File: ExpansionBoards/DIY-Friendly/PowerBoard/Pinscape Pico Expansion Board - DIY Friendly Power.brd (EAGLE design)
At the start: 138 x 100 mm, 79 parts, among them IC1 UCC27524P, IC10 ULN2803A, IC11 ULN2803A, IC12 ULN2803A, IC13 DS1307+, IC2 UCC27524P, IC3 UCC27524P, IC4 UCC27524P, IC5 UCC27524P, IC6 UCC27524P, IC7 UCC27524P, IC8 UCC27524P, IC9 ULN2803A, J1 640445-4, J15 SSQ-108-02-T-S-RA, J2 640445-9, J3 640445-9, J4 1-640456-0, J5 1-640456-0, J6 1-640456-0, J7 1-640456-0, Q1 FDPF085N10A, Q10 FDPF085N10A, Q11 FDPF085N10A, Q12 FDPF085N10A, Q13 FDPF085N10A, Q14 FDPF085N10A, Q15 FDPF085N10A, Q16 FDPF085N10A, Q2 FDPF085N10A, Q3 FDPF085N10A, Q4 FDPF085N10A, Q5 FDPF085N10A, Q6 FDPF085N10A, Q7 FDPF085N10A, Q8 FDPF085N10A, Q9 FDPF085N10A, Y1 ECS-.327-12.5-13X-C

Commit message: expansion board improvements
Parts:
- J1: value 640445-4 -> 640445-6; device SamacSys_Parts:SHDR4W117P0X396_1X4_1585X762X1 -> SamacSys_Parts:SHDR6W183P0X396_1X6_2377X762X1
- moved J1 13.5 mm to (105.8, 93.7), turned to 0 degrees
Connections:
- net 12V: now also J1.5; no longer J1.3
- net 5V: now also J1.6; no longer J1.4
- net GND: now also J1.3, J1.4
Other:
- board text added: "REV 20250106"
- board text removed: "REV 20241208"
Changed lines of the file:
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@@
 PICO</text>
 <text x="8.5" y="52.5" size="1.1" layer="25" ratio="20" rot="SR0" align="center">DIY POWER BOARD</text>
-<text x="8.4" y="51" size="1.1" layer="25" ratio="15" rot="SR0" align="center">REV 20241208</text>
+<text x="8.4" y="51" size="1.1" layer="25" ratio="15" rot="SR0" align="center">REV 20250106</text>
 <text x="29.5" y="98.3" size="1.8" layer="25" ratio="15" rot="SR0" align="center">HIGH POWER OUTPUTS 13-20</text>
 <text x="33.8" y="53.5" size="1.8" layer="25" ratio="15" rot="SR0" align="center">PICO 1</text>
@@
 <text x="80.7" y="98.4" size="1.8" layer="25" ratio="15" rot="SR0" align="center">HIGH POWER OUTPUTS 21-28</text>
 <text x="80.4" y="87.8" size="2.5" layer="25" ratio="15" rot="SR270" align="center">X</text>
-<text x="119.4" y="98.2" size="1.8" layer="25" ratio="15" rot="SR0" align="center">2ND PSU</text>
+<text x="116.5" y="98.4" size="1.8" layer="25" ratio="15" rot="SR0" align="center">2ND PSU</text>
 <text x="122.3" y="87.7" size="1.5" layer="25" ratio="15" rot="SR0" align="center">12V</text>
-<text x="117.6" y="87.7" size="1.5" layer="25" ratio="15" rot="SR0" align="center">GND</text>
+<text x="110" y="87.8" size="1.2" layer="25" ratio="15" rot="SR0" align="center">GND</text>
 <text x="12.4" y="31.4" size="1.8" layer="25" ratio="15" rot="SR270" align="center">TO MAIN BOARD</text>
 <text x="136.2" y="76.7" size="1.8" layer="25" ratio="15" rot="SR90" align="center">LAMPS 1-8</text>
@@
 <text x="91.5" y="9.6" size="1.2" layer="25" ratio="15" rot="SR0" align="center">32</text>
 <text x="127.6" y="35.5" size="1.4" layer="25" ratio="15" rot="SR0" align="center">5V</text>
-<text x="112.9" y="87.7" size="1.5" layer="25" ratio="15" rot="SR0" align="center">GND</text>
+<text x="105.7" y="87.8" size="1.2" layer="25" ratio="15" rot="SR0" align="center">GND</text>
 <text x="101.6" y="49.3" size="2" layer="21" align="center">CR2032</text>
 <text x="18" y="88.3" size="1.2" layer="25" ratio="15" rot="SR0" align="center">14</text>
@@
 <text x="99.3" y="9.6" size="1.2" layer="25" ratio="15" rot="SR0" align="center">30</text>
 <text x="96.8" y="9.6" size="1.2" layer="25" ratio="15" rot="SR0" align="center">31</text>
+<text x="114" y="87.8" size="1.2" layer="25" ratio="15" rot="SR0" align="center">GND</text>
+<text x="118" y="87.8" size="1.2" layer="25" ratio="15" rot="SR0" align="center">GND</text>
 </plain>
 <attributes>
@@
 <attribute name="VALUE" x="81.478" y="62.667" size="0.6" layer="27" ratio="10" rot="R180"/>
 </element>
-<element name="J1" library="SamacSys_Parts" package="SHDR4W117P0X396_1X4_1585X762X1" value="640445-4" x="119.3" y="93.7" smashed="yes" rot="R180">
-<attribute name="MOUSER_PRICE-STOCK" value="https://www.mouser.co.uk/ProductDetail/TE-Connectivity-AMP/640445-4?qs=P8zzrVhehatZnQ7HMsIjxw%3D%3D" x="119.3" y="93.7" size="1" layer="27" rot="R180" display="off"/>
-<attribute name="HEIGHT" value="13.716mm" x="119.3" y="93.7" size="1" layer="27" rot="R180" display="off"/>
-<attribute name="MANUFACTURER_PART_NUMBER" value="640445-4" x="119.3" y="93.7" size="1" layer="27" rot="R180" display="off"/>
-<attribute name="MANUFACTURER_NAME" value="TE Connectivity" x="119.3" y="93.7" size="1" layer="27" rot="R180" display="off"/>
-<attribute name="MOUSER_PART_NUMBER" value="571-6404454" x="119.3" y="93.7" size="1" layer="27" rot="R180" display="off"/>
-<attribute name="DESCRIPTION" value="Conn Wire to Board HDR 4 POS 3.96mm Solder ST Top Entry Thru-Hole Package" x="119.3" y="93.7" size="1" layer="27" rot="R180" display="off"/>
-<attribute name="NAME" x="122.3" y="91.4" size="1.27" layer="25" rot="R270" align="center"/>
-<attribute name="VALUE" x="114.5" y="91.2" size="0.8" layer="27" rot="R180" align="center"/>
+<element name="J1" library="SamacSys_Parts" package="SHDR6W183P0X396_1X6_2377X762X1" value="640445-6" x="105.8" y="93.7" smashed="yes">
+<attribute name="MOUSER_PRICE-STOCK" value="https://www.mouser.com/Search/Refine.aspx?Keyword=571-6404456" x="105.8" y="93.7" size="1" layer="27" display="off"/>
+<attribute name="HEIGHT" value="11.049mm" x="105.8" y="93.7" size="1" layer="27" display="off"/>
+<attribute name="MANUFACTURER_PART_NUMBER" value="640445-6" x="105.8" y="93.7" size="1" layer="27" display="off"/>
+<attribute name="MANUFACTURER_NAME" value="TE Connectivity" x="105.8" y="93.7" size="1" layer="27" display="off"/>
+<attribute name="MOUSER_PART_NUMBER" value="571-6404456" x="105.8" y="93.7" size="1" layer="27" display="off"/>
+<attribute name="DESCRIPTION" value="6 way friction lock header,3.96mm pitch" x="105.8" y="93.7" size="1" layer="27" display="off"/>
+<attribute name="NAME" x="105" y="97.8" size="1.27" layer="25" rot="R180" align="center"/>
+<attribute name="VALUE" x="110.6" y="96.2" size="0.8" layer="27" align="center"/>
 </element>
 <element name="J15" library="SamacSys_Parts" package="RHDRRA8W64P254_1X8_2083X851X24" value="SSQ-108-02-T-S-RA" x="9.9" y="40.1" smashed="yes" rot="R90">
@@
 <via x="106.8" y="45.4" extent="1-16" drill="0.45"/>
 <via x="105.9" y="27.1" extent="1-16" drill="0.45"/>
+<contactref element="J1" pad="3"/>
+<contactref element="J1" pad="4"/>
+<polygon width="0.3" layer="1" thermals="no">
+<vertex x="103.6" y="95.7"/>
+<vertex x="119.6" y="95.7"/>
+<vertex x="119.6" y="91.6"/>
+<vertex x="103.6" y="91.6"/>
+</polygon>
+<polygon width="0.3" layer="16" thermals="no">
+<vertex x="103.6" y="91.6"/>
+<vertex x="119.6" y="91.6"/>
+<vertex x="119.6" y="95.7"/>
+<vertex x="103.6" y="95.7"/>
+</polygon>
+<polygon width="0.3" layer="16" thermals="no">
+<vertex x="12" y="23.5"/>
+<vertex x="12" y="41.5"/>
+<vertex x="7.9" y="41.5"/>
+<vertex x="7.9" y="23.5"/>
+</polygon>
+<polygon width="0.3" layer="1" thermals="no">
+<vertex x="7.9" y="23.6"/>
+<vertex x="7.9" y="41.5"/>
+<vertex x="12" y="41.5"/>
+<vertex x="12" y="23.6"/>
+</polygon>
 </signal>
 <signal name="SDA">
@@
 <wire x1="128.7" y1="12.7" x2="121.4" y2="5.4" width="2" layer="16"/>
 <wire x1="114.33" y1="5.4" x2="121.4" y2="5.4" width="2" layer="16"/>
-<contactref element="J1" pad="4"/>
-<wire x1="125.246" y1="93.7" x2="125.246" y2="91.984" width="2" layer="1"/>
-<wire x1="125.246" y1="91.984" x2="129.4" y2="87.83" width="2" layer="1"/>
 <contactref element="IC13" pad="8"/>
+<wire x1="125.6" y1="91.63" x2="129.4" y2="87.83" width="2" layer="1"/>
 <wire x1="58.1" y1="0.6" x2="112.3" y2="0.6" width="0.4" layer="1"/>
 <wire x1="112.3" y1="0.6" x2="114.33" y2="2.63" width="0.4" layer="1"/>
@@
 <wire x1="52.7" y1="6" x2="58.1" y2="0.6" width="0.4" layer="1"/>
 <wire x1="53.99" y1="24.39" x2="52.7" y2="23.1" width="0.4" layer="1"/>
+<contactref element="J1" pad="6"/>
+<wire x1="125.6" y1="93.7" x2="125.6" y2="91.63" width="2" layer="1"/>
 </signal>
 <signal name="SDA1">
@@
 <wire x1="70.09" y1="66.72" x2="71.5" y2="68.13" width="1" layer="1"/>
 <wire x1="80.5" y1="68.13" x2="80.5" y2="66.17" width="1" layer="1"/>
-<contactref element="J1" pad="3"/>
 <contactref element="IC7" pad="6"/>
 <contactref element="IC7" pad="8"/>
@@
 <wire x1="107.73" y1="68.13" x2="108.7" y2="69.1" width="1" layer="1"/>
 <wire x1="108.7" y1="69.1" x2="108.7" y2="76.7" width="1" layer="1"/>
-<wire x1="108.7" y1="76.7" x2="120.4" y2="88.4" width="1" layer="1"/>
-<wire x1="120.4" y1="88.4" x2="120.624" y2="88.624" width="1" layer="1"/>
-<wire x1="121.284" y1="93.7" x2="121.284" y2="89.284" width="1" layer="1"/>
-<wire x1="121.284" y1="89.284" x2="120.624" y2="88.624" width="1" layer="1"/>
+<wire x1="108.7" y1="76.7" x2="120.95" y2="88.95" width="1" layer="1"/>
+<contactref element="J1" pad="5"/>
+<wire x1="120.95" y1="88.95" x2="121.284" y2="89.284" width="1" layer="1"/>
+<wire x1="121.64" y1="93.7" x2="121.64" y2="89.64" width="1" layer="1"/>
+<wire x1="121.64" y1="89.64" x2="121.284" y2="89.284" width="1" layer="1"/>
 </signal>
 <signal name="OUTCTL14">
@@
 <wire x1="99.64" y1="81.4" x2="102.1" y2="81.4" width="2.5" layer="1"/>
 <wire x1="102.1" y1="81.4" x2="103" y2="82.3" width="2.5" layer="1"/>
-<wire x1="103" y1="82.3" x2="103" y2="87" width="2.5" layer="1"/>
-<wire x1="96.494" y1="93.7" x2="96.494" y2="91.706" width="2.5" layer="1"/>
-<wire x1="96.494" y1="91.706" x2="99.5" y2="88.7" width="2.5" layer="1"/>
-<wire x1="99.5" y1="88.7" x2="101.3" y2="88.7" width="2.5" layer="1"/>
-<wire x1="101.3" y1="88.7" x2="103" y2="87" width="2.5" layer="1"/>
+<wire x1="96.494" y1="93.7" x2="96.494" y2="89.706" width="2.5" layer="1"/>
+<wire x1="96.494" y1="89.706" x2="99.4" y2="86.8" width="2.5" layer="1"/>
+<wire x1="99.4" y1="86.8" x2="101.3" y2="86.8" width="2.5" layer="1"/>
+<wire x1="101.3" y1="86.8" x2="103" y2="85.1" width="2.5" layer="1"/>
+<wire x1="103" y1="82.3" x2="103" y2="85.1" width="2.5" layer="1"/>
 </signal>
 <signal name="OUT28">
@@
 <wire x1="106.44" y1="81.4" x2="108.5" y2="81.4" width="2.5" layer="1"/>
 <wire x1="108.5" y1="81.4" x2="109.9" y2="82.8" width="2.5" layer="1"/>
-<wire x1="109.9" y1="82.8" x2="109.9" y2="86.9" width="2.5" layer="1"/>
-<wire x1="100.456" y1="93.7" x2="103.1" y2="93.7" width="2.5" layer="1"/>
-<wire x1="103.1" y1="93.7" x2="109.9" y2="86.9" width="2.5" layer="1"/>
+<wire x1="109.9" y1="82.8" x2="109.9" y2="85.3" width="2.5" layer="1"/>
+<wire x1="100.456" y1="93.7" x2="100.456" y2="92.144" width="2.5" layer="1"/>
+<wire x1="100.456" y1="92.144" x2="105.7" y2="86.9" width="2.5" layer="1"/>
+<wire x1="105.7" y1="86.9" x2="108.3" y2="86.9" width="2.5" layer="1"/>
+<wire x1="108.3" y1="86.9" x2="109.9" y2="85.3" width="2.5" layer="1"/>
 </signal>
 <signal name="N$21">

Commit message: add logo image
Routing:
- net GND: track 0.00 -> 17.1 mm
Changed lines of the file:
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@@
 <contactref element="J1" pad="3"/>
 <contactref element="J1" pad="4"/>
-<polygon width="0.3" layer="1" thermals="no">
-<vertex x="103.6" y="95.7"/>
-<vertex x="119.6" y="95.7"/>
-<vertex x="119.6" y="91.6"/>
-<vertex x="103.6" y="91.6"/>
-</polygon>
-<polygon width="0.3" layer="16" thermals="no">
-<vertex x="103.6" y="91.6"/>
-<vertex x="119.6" y="91.6"/>
-<vertex x="119.6" y="95.7"/>
-<vertex x="103.6" y="95.7"/>
-</polygon>
 <polygon width="0.3" layer="16" thermals="no">
 <vertex x="12" y="23.5"/>
@@
 <vertex x="12" y="23.6"/>
 </polygon>
+<wire x1="105.8" y1="93.7" x2="105.8" y2="91.6" width="1.5" layer="1"/>
+<wire x1="109.76" y1="93.7" x2="109.76" y2="91.64" width="1.5" layer="1"/>
+<wire x1="113.72" y1="93.7" x2="113.72" y2="91.68" width="1.5" layer="1"/>
+<wire x1="117.68" y1="93.7" x2="117.68" y2="91.72" width="1.5" layer="1"/>
+<wire x1="105.8" y1="93.7" x2="105.8" y2="91.4" width="1.5" layer="16"/>
+<wire x1="109.76" y1="93.7" x2="109.76" y2="91.24" width="1.5" layer="16"/>
+<wire x1="113.72" y1="93.7" x2="113.72" y2="91.58" width="1.5" layer="16"/>
+<wire x1="117.68" y1="93.7" x2="117.68" y2="91.62" width="1.5" layer="16"/>
 </signal>
 <signal name="SDA">

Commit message: minor board updates
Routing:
- net GND: track 17.1 -> 33.1 mm, vias 16 -> 17
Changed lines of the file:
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@@
 <contactref element="J1" pad="3"/>
 <contactref element="J1" pad="4"/>
-<polygon width="0.3" layer="16" thermals="no">
-<vertex x="12" y="23.5"/>
-<vertex x="12" y="41.5"/>
-<vertex x="7.9" y="41.5"/>
-<vertex x="7.9" y="23.5"/>
-</polygon>
-<polygon width="0.3" layer="1" thermals="no">
-<vertex x="7.9" y="23.6"/>
-<vertex x="7.9" y="41.5"/>
-<vertex x="12" y="41.5"/>
-<vertex x="12" y="23.6"/>
-</polygon>
 <wire x1="105.8" y1="93.7" x2="105.8" y2="91.6" width="1.5" layer="1"/>
 <wire x1="109.76" y1="93.7" x2="109.76" y2="91.64" width="1.5" layer="1"/>
@@
 <wire x1="113.72" y1="93.7" x2="113.72" y2="91.58" width="1.5" layer="16"/>
 <wire x1="117.68" y1="93.7" x2="117.68" y2="91.62" width="1.5" layer="16"/>
+<wire x1="9.9" y1="35.02" x2="7.8" y2="35.02" width="1.5" layer="16"/>
+<wire x1="9.9" y1="29.94" x2="7.8" y2="29.94" width="1.5" layer="16"/>
+<wire x1="9.9" y1="24.86" x2="7.9" y2="24.86" width="1.5" layer="16"/>
+<wire x1="9.9" y1="24.86" x2="8" y2="24.86" width="1.5" layer="1"/>
+<wire x1="9.9" y1="29.94" x2="7.8" y2="29.94" width="1.5" layer="1"/>
+<wire x1="9.9" y1="35.02" x2="7.7" y2="35.02" width="1.5" layer="1"/>
+<wire x1="9.9" y1="40.1" x2="9.5" y2="40.1" width="1.5" layer="1"/>
+<wire x1="9.5" y1="40.1" x2="7.9" y2="40.1" width="1.5" layer="1"/>
+<via x="9.5" y="40.1" extent="1-16" drill="0.45"/>
+<wire x1="9.5" y1="40.1" x2="7.9" y2="40.1" width="1.5" layer="16"/>
 </signal>
 <signal name="SDA">

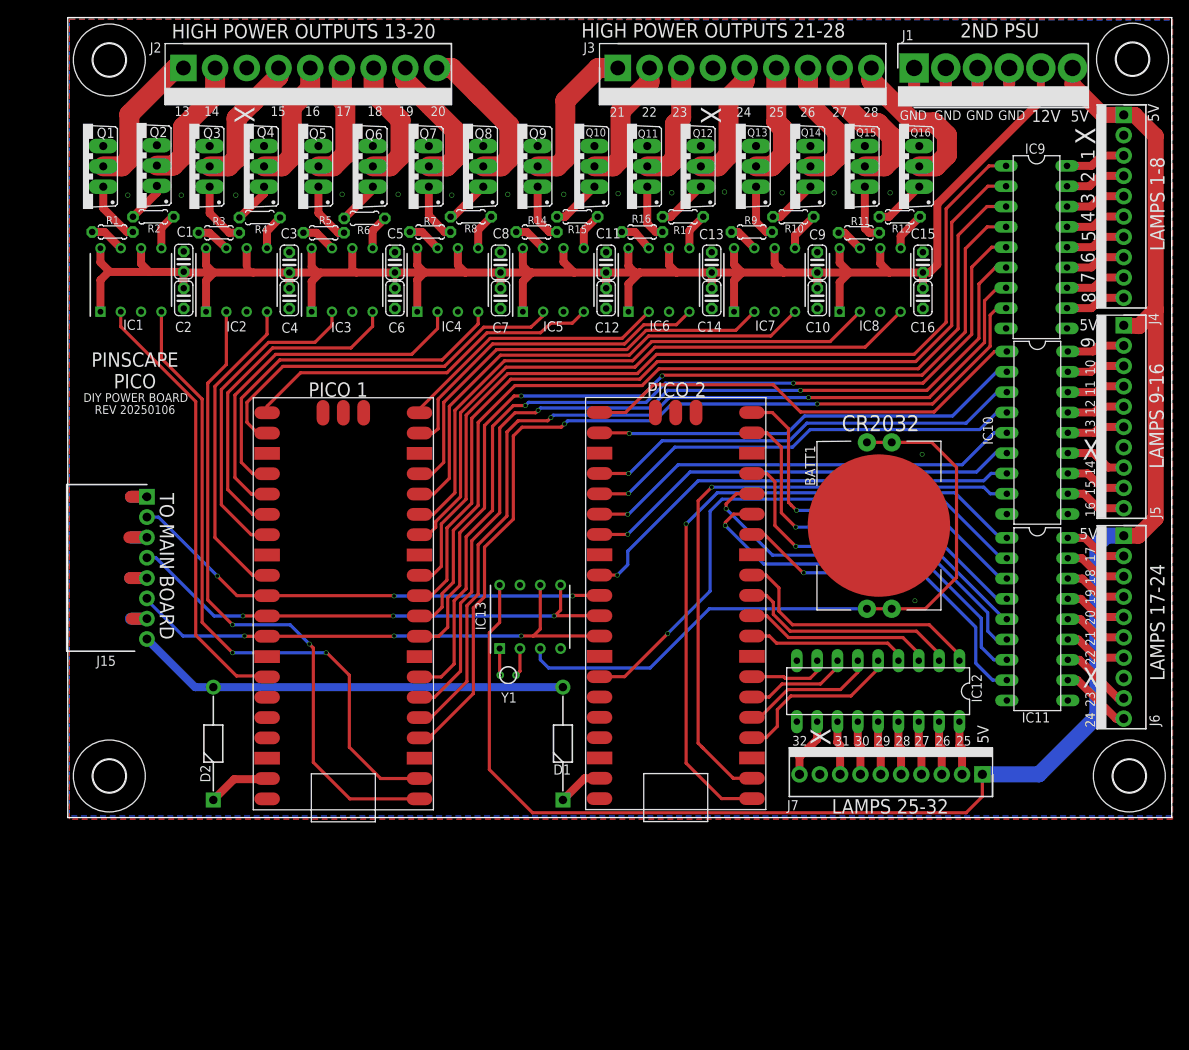
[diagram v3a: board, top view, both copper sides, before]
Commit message: DIY board: individual reset buttons per Pico; swap cross-board connectors
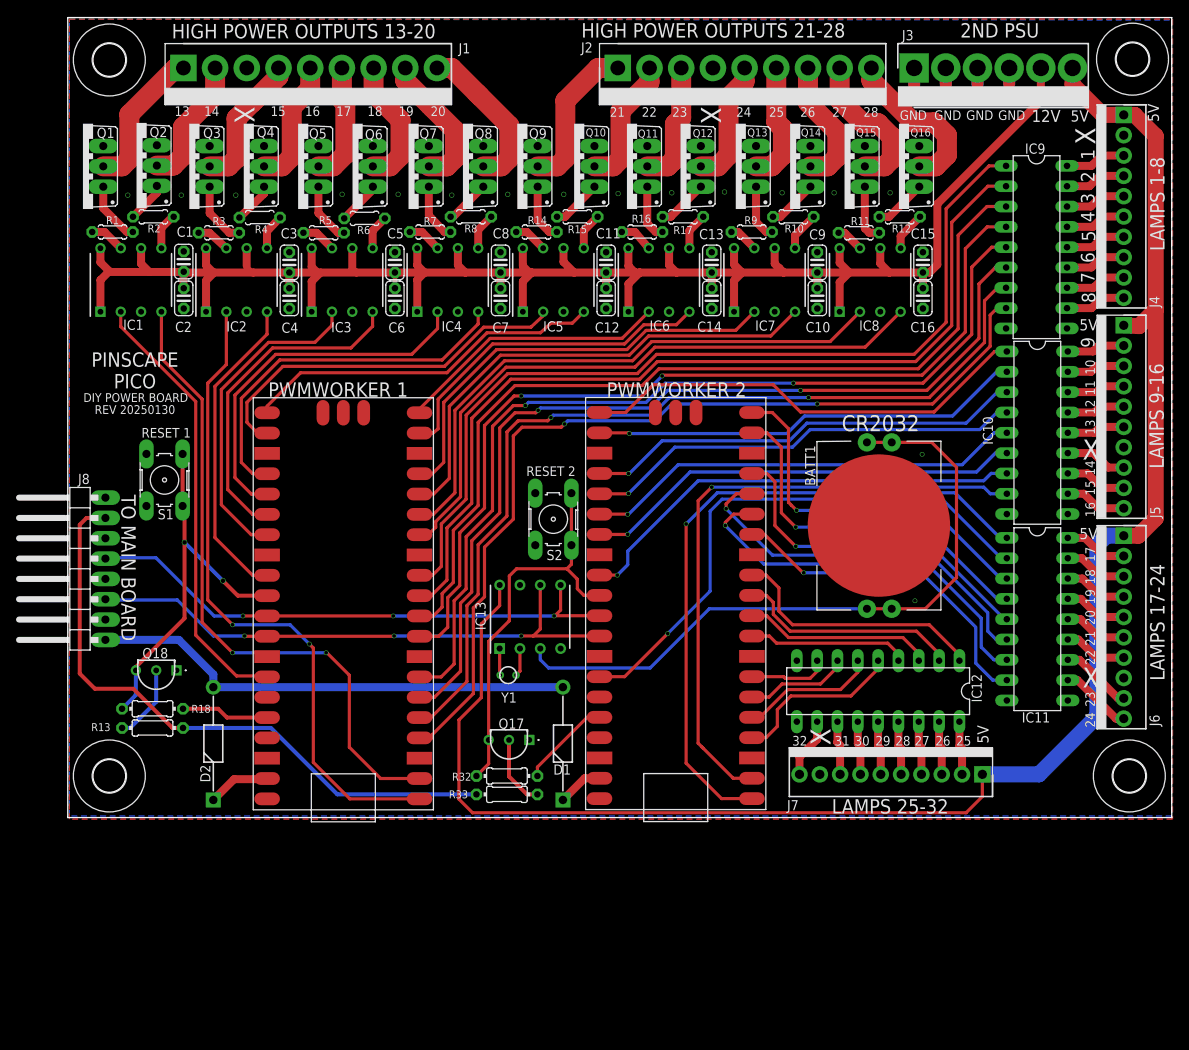
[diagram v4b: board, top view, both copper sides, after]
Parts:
- removed J15: SSQ-108-02-T-S-RA, SamacSys_Parts:RHDRRA8W64P254_1X8_2083X851X24
- added J8: (no value), pinhead:1X08/90
- added Q17, Q18: 2N2222A, SamacSys_Parts:2N2222A
- added R13, R33: 2.2k, resistor:0204/7
- added R18, R32: 4.7K, resistor:0204/7
- added S1, S2: (no value), switch-omron:B3F-10XX
- J1: value 640445-6 -> 640445-9; device SamacSys_Parts:SHDR6W183P0X396_1X6_2377X762X1 -> SamacSys_Parts:SHDR9W117P0X396_1X9_3566X762X1
- J3: value 640445-9 -> 640445-6; device SamacSys_Parts:SHDR9W117P0X396_1X9_3566X762X1 -> SamacSys_Parts:SHDR6W183P0X396_1X6_2377X762X1
- moved J1 75.5 mm to (30.3, 93.7), turned to 180 degrees
- moved J2 54.3 mm to (84.6, 93.7)
- moved J3 21.2 mm to (105.8, 93.7), turned to 0 degrees
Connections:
- removed net /RESET: J15.2, PICO1.RUN, PICO2.RUN
- new net /PERIPHERAL_POWER_ENABLE: J8.7, R13.1, R33.1
- new net N$38: PICO2.3V3, R32.2
- new net N$39: Q17.2, R33.2
- new net N$40: PICO2.RUN, Q17.3, R32.1, S2.3, S2.4
- new net N$41: PICO1.3V3, R18.2
- new net N$42: Q18.2, R13.2
- new net N$51: PICO1.RUN, Q18.3, R18.1, S1.3, S1.4
- net 12V: now also J3.5; no longer J1.5
- net 5V: now also J3.6; no longer J1.6
- net GND: now also J3.1, J3.2, J3.3, J3.4, J8.2, J8.4, J8.6, J8.8, Q17.1, Q18.1, S1.1, S1.2, S2.1, S2.2; no longer J1.1, J1.2, J1.3, J1.4, J15.1, J15.3, J15.5, J15.7
- net OUT13: now also J1.1; no longer J2.1
- net OUT14: now also J1.2; no longer J2.2
- net OUT15: now also J1.4; no longer J2.4
- net OUT16: now also J1.5; no longer J2.5
- net OUT17: now also J1.6; no longer J2.6
- net OUT18: now also J1.7; no longer J2.7
- net OUT19: now also J1.8; no longer J2.8
- net OUT20: now also J1.9; no longer J2.9
- net OUT21: now also J2.1; no longer J3.1
- net OUT22: now also J2.2; no longer J3.2
- net OUT23: now also J2.3; no longer J3.3
- net OUT24: now also J2.5; no longer J3.5
- net OUT25: now also J2.6; no longer J3.6
- net OUT26: now also J2.7; no longer J3.7
- net OUT27: now also J2.8; no longer J3.8
- net OUT28: now also J2.9; no longer J3.9
- net SCL: now also J8.3; no longer J15.6
- net SDA: now also J8.5; no longer J15.4
- net VBUS: now also J8.1; no longer J15.8
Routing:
- net /PERIPHERAL_POWER_ENABLE: track 0.00 -> 78.0 mm
- net /RESET: track 60.7 -> 0.00 mm, vias 3 -> 0
- net N$40: track 0.00 -> 50.1 mm
- net N$51: track 0.00 -> 48.3 mm, vias 0 -> 2
- net GND: track 33.1 -> 17.1 mm, vias 17 -> 16
- net N$38: track 0.00 -> 11.5 mm
- net N$41: track 0.00 -> 11.0 mm
- net N$42: track 0.00 -> 9.56 mm
- net N$39: track 0.00 -> 9.04 mm
- net 5V: track 206.3 -> 213.9 mm
- net VBUS: track 54.5 -> 60.6 mm
- net SDA: track 63.7 -> 69.0 mm
- net SCL: track 65.4 -> 70.4 mm
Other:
- board text added: "PWMWORKER 1"
- board text added: "PWMWORKER 2"
- board text added: "RESET 1"
- board text added: "RESET 2"
- board text added: "REV 20250130"
- board text removed: "PICO 1"
- board text removed: "PICO 2"
- board text removed: "REV 20250106"
